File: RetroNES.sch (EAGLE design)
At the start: 8 parts, among them IC1 ATMEGA32U4-AU

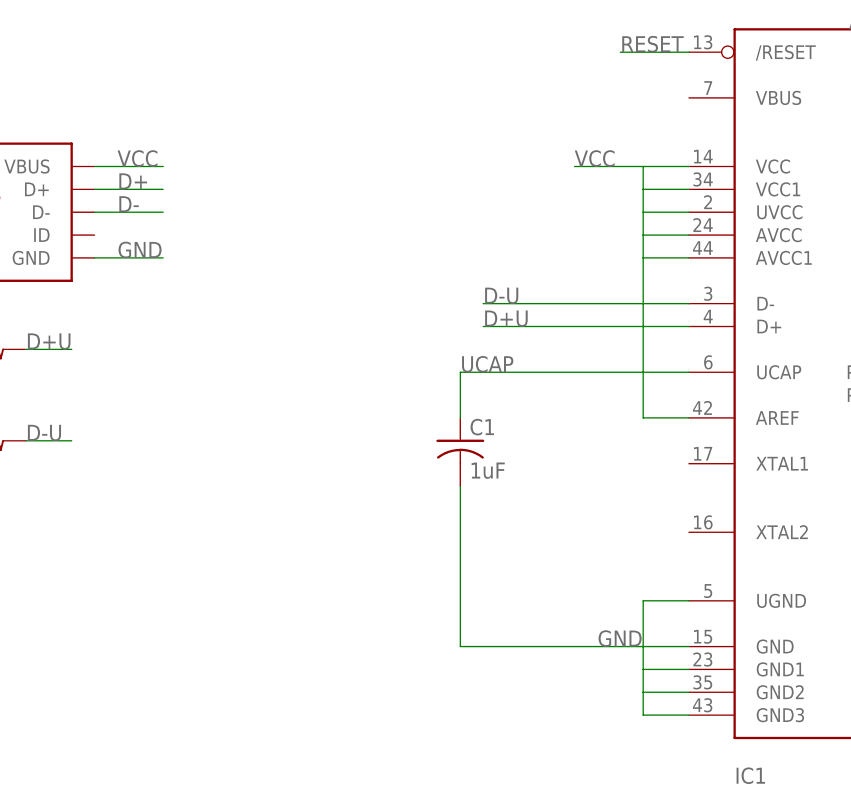
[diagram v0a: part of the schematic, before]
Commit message: Added the source code.
The source code is essentially the same as the retropad project and
massaged to make it work with hard wired buttons.
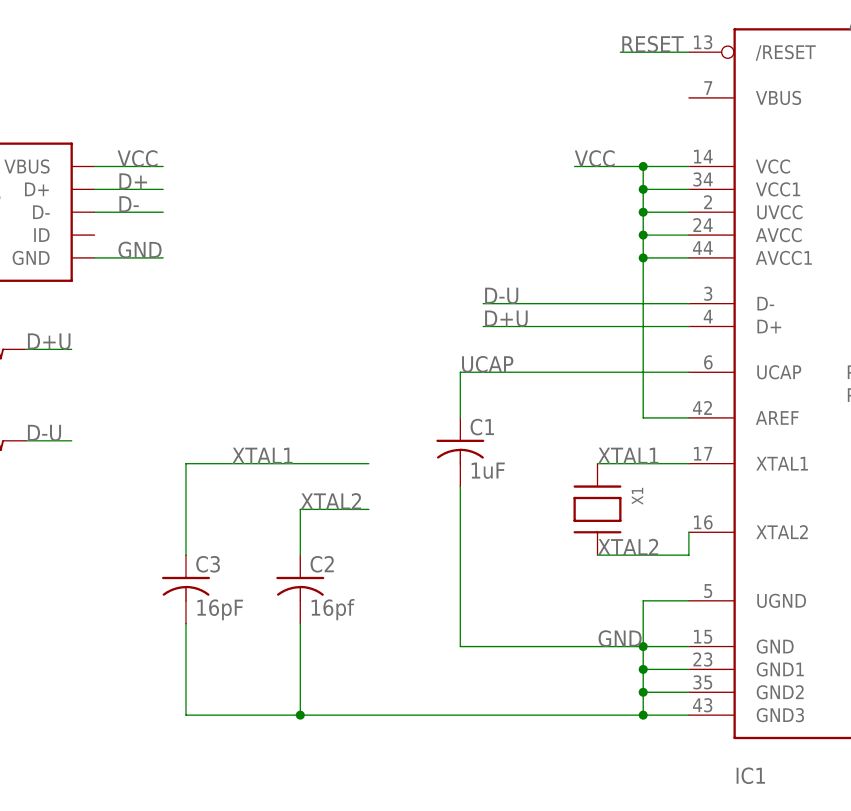
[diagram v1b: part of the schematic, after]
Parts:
- added C2: 16pf, adafruit:C-USC0805
- added C3: 16pF, adafruit:C-USC0805
- added X1: (no value), adafruit:XTAL-3.2X1.5
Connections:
- new net XTAL1: C3.1, IC1.XTAL1, X1.P$1
- new net XTAL2: C2.1, IC1.XTAL2, X1.P$2
- net GND: now also C2.2, C3.2
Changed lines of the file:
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@@
 <?xml version="1.0" encoding="utf-8"?>
 <!DOCTYPE eagle SYSTEM "eagle.dtd">
-<eagle version="6.3">
+<eagle version="7.1.0">
 <drawing>
 <settings>
@@
 <layer number="54" name="bGND_GNDA" color="1" fill="9" visible="no" active="no"/>
 <layer number="56" name="wert" color="7" fill="1" visible="no" active="no"/>
+<layer number="57" name="tCAD" color="7" fill="1" visible="no" active="no"/>
 <layer number="91" name="Nets" color="2" fill="1" visible="yes" active="yes"/>
 <layer number="92" name="Busses" color="1" fill="1" visible="yes" active="yes"/>
@@
 <layer number="97" name="Info" color="7" fill="1" visible="yes" active="yes"/>
 <layer number="98" name="Guide" color="6" fill="1" visible="yes" active="yes"/>
+<layer number="99" name="SpiceOrder" color="7" fill="1" visible="no" active="no"/>
 <layer number="100" name="Muster" color="7" fill="1" visible="no" active="no"/>
 <layer number="101" name="Patch_Top" color="12" fill="4" visible="yes" active="yes"/>
@@
 <layer number="109" name="fp9" color="7" fill="1" visible="no" active="yes"/>
 <layer number="110" name="fp0" color="7" fill="1" visible="no" active="yes"/>
+<layer number="111" name="LPC17xx" color="7" fill="1" visible="no" active="yes"/>
+<layer number="112" name="tSilk" color="7" fill="1" visible="no" active="yes"/>
+<layer number="113" name="ReferenceLS" color="7" fill="1" visible="no" active="no"/>
 <layer number="116" name="Patch_BOT" color="9" fill="4" visible="yes" active="yes"/>
+<layer number="118" name="Rect_Pads" color="7" fill="1" visible="no" active="no"/>
 <layer number="121" name="_tsilk" color="7" fill="1" visible="yes" active="yes"/>
 <layer number="122" name="_bsilk" color="7" fill="1" visible="yes" active="yes"/>
@@
 <layer number="124" name="bTestmark" color="7" fill="1" visible="no" active="yes"/>
 <layer number="125" name="_tNames" color="7" fill="1" visible="yes" active="yes"/>
+<layer number="126" name="_bNames" color="7" fill="1" visible="no" active="yes"/>
+<layer number="127" name="_tValues" color="7" fill="1" visible="no" active="yes"/>
+<layer number="128" name="_bValues" color="7" fill="1" visible="no" active="yes"/>
 <layer number="131" name="tAdjust" color="7" fill="1" visible="no" active="yes"/>
 <layer number="132" name="bAdjust" color="7" fill="1" visible="no" active="yes"/>
 <layer number="144" name="Drill_legend" color="7" fill="1" visible="yes" active="yes"/>
+<layer number="150" name="Notes" color="7" fill="1" visible="no" active="yes"/>
 <layer number="151" name="HeatSink" color="7" fill="1" visible="yes" active="yes"/>
+<layer number="152" name="_bDocu" color="7" fill="1" visible="no" active="yes"/>
+<layer number="153" name="FabDoc1" color="6" fill="1" visible="no" active="no"/>
+<layer number="154" name="FabDoc2" color="2" fill="1" visible="no" active="no"/>
+<layer number="155" name="FabDoc3" color="7" fill="15" visible="no" active="no"/>
 <layer number="199" name="Contour" color="7" fill="1" visible="yes" active="yes"/>
 <layer number="200" name="200bmp" color="1" fill="10" visible="yes" active="yes"/>
@@
 <layer number="223" name="223bmp" color="24" fill="1" visible="no" active="no"/>
 <layer number="224" name="224bmp" color="25" fill="1" visible="no" active="no"/>
+<layer number="231" name="Eagle3D_PG1" color="7" fill="1" visible="no" active="no"/>
+<layer number="232" name="Eagle3D_PG2" color="7" fill="1" visible="no" active="no"/>
+<layer number="233" name="Eagle3D_PG3" color="7" fill="1" visible="no" active="no"/>
+<layer number="248" name="Housing" color="7" fill="1" visible="no" active="yes"/>
+<layer number="249" name="Edge" color="7" fill="1" visible="no" active="yes"/>
 <layer number="250" name="Descript" color="7" fill="1" visible="no" active="no"/>
 <layer number="251" name="SMDround" color="7" fill="1" visible="no" active="no"/>
@@
 <part name="NES" library="RetroNES" deviceset="NES_SOCKET" device=""/>
 <part name="WII" library="RetroNES" deviceset="WII_PADS" device=""/>
+<part name="C2" library="adafruit" deviceset="C-US" device="C0805" value="16pf"/>
+<part name="C3" library="adafruit" deviceset="C-US" device="C0805" value="16pF"/>
+<part name="X1" library="adafruit" deviceset="XTAL" device="-3.2X1.5"/>
 </parts>
 <sheets>
@@
 <instance part="NES" gate="G$1" x="165.1" y="160.02"/>
 <instance part="WII" gate="G$1" x="162.56" y="109.22"/>
+<instance part="C2" gate="G$1" x="25.4" y="43.18"/>
+<instance part="C3" gate="G$1" x="12.7" y="43.18"/>
+<instance part="X1" gate="G$1" x="58.42" y="50.8" rot="R270"/>
 </instances>
 <busses>
@@
 <wire x1="63.5" y1="35.56" x2="43.18" y2="35.56" width="0.1524" layer="91"/>
 <wire x1="43.18" y1="35.56" x2="43.18" y2="53.34" width="0.1524" layer="91"/>
+<pinref part="C3" gate="G$1" pin="2"/>
+<wire x1="12.7" y1="38.1" x2="12.7" y2="27.94" width="0.2032" layer="91"/>
+<wire x1="12.7" y1="27.94" x2="25.4" y2="27.94" width="0.2032" layer="91"/>
+<pinref part="C2" gate="G$1" pin="2"/>
+<wire x1="25.4" y1="27.94" x2="63.5" y2="27.94" width="0.2032" layer="91"/>
+<wire x1="25.4" y1="38.1" x2="25.4" y2="27.94" width="0.2032" layer="91"/>
+<junction x="25.4" y="27.94"/>
+<junction x="63.5" y="27.94"/>
+<junction x="63.5" y="35.56"/>
+<junction x="63.5" y="33.02"/>
+<junction x="63.5" y="30.48"/>
 </segment>
 <segment>
@@
 <wire x1="63.5" y1="88.9" x2="55.88" y2="88.9" width="0.1524" layer="91"/>
 <label x="55.88" y="88.9" size="1.778" layer="95"/>
+<junction x="63.5" y="86.36"/>
+<junction x="63.5" y="83.82"/>
+<junction x="63.5" y="81.28"/>
+<junction x="63.5" y="78.74"/>
+<junction x="63.5" y="88.9"/>
 </segment>
 <segment>
@@
 </segment>
 </net>
+<net name="XTAL1" class="0">
+<segment>
+<pinref part="IC1" gate="G$1" pin="XTAL1"/>
+<pinref part="X1" gate="G$1" pin="P$1"/>
+<wire x1="68.58" y1="55.88" x2="58.42" y2="55.88" width="0.2032" layer="91"/>
+<label x="58.42" y="55.88" size="1.778" layer="95"/>
+</segment>
+<segment>
+<pinref part="C3" gate="G$1" pin="1"/>
+<wire x1="12.7" y1="45.72" x2="12.7" y2="55.88" width="0.2032" layer="91"/>
+<wire x1="12.7" y1="55.88" x2="33.02" y2="55.88" width="0.2032" layer="91"/>
+<label x="17.78" y="55.88" size="1.778" layer="95"/>
+</segment>
+</net>
+<net name="XTAL2" class="0">
+<segment>
+<pinref part="IC1" gate="G$1" pin="XTAL2"/>
+<wire x1="68.58" y1="48.26" x2="68.58" y2="45.72" width="0.2032" layer="91"/>
+<pinref part="X1" gate="G$1" pin="P$2"/>
+<wire x1="68.58" y1="45.72" x2="58.42" y2="45.72" width="0.2032" layer="91"/>
+<label x="58.42" y="45.72" size="1.778" layer="95"/>
+</segment>
+<segment>
+<pinref part="C2" gate="G$1" pin="1"/>
+<wire x1="25.4" y1="45.72" x2="25.4" y2="50.8" width="0.2032" layer="91"/>
+<wire x1="25.4" y1="50.8" x2="33.02" y2="50.8" width="0.2032" layer="91"/>
+<label x="25.4" y="50.8" size="1.778" layer="95"/>
+</segment>
+</net>
 </nets>
 </sheet>
 </sheets>
+<errors>
+</errors>
 </schematic>
 </drawing>
